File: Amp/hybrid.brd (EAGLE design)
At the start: 172.7 x 137.2 mm, 139 parts, among them IC1 TL071P, IC2 TL071P, IC3 LM317MABT, IC4 LM317MABT, J1 NRJ3HF-1, K1 UA2-12NJ, Q1 KSP06KINKED, Q10 BD139, Q11 KSP06KINKED, Q12 BC560KINKED, Q13 BC560KINKED, Q14 BC560KINKED, Q15 BC556KINKED, Q16 BC550KINKED, Q17 BC550KINKED, Q18 BC560KINKED, Q19 BD140, Q2 BC560KINKED, Q20 BD139, Q21 KSP43, Q22 KSP43, Q23 BC546KINKED, Q3 BC560KINKED, Q4 BC560KINKED, Q5 BC556KINKED, Q6 BC550KINKED, Q7 BC550KINKED, Q8 BC560KINKED, Q9 BD140, U1 TL7700DIP-8

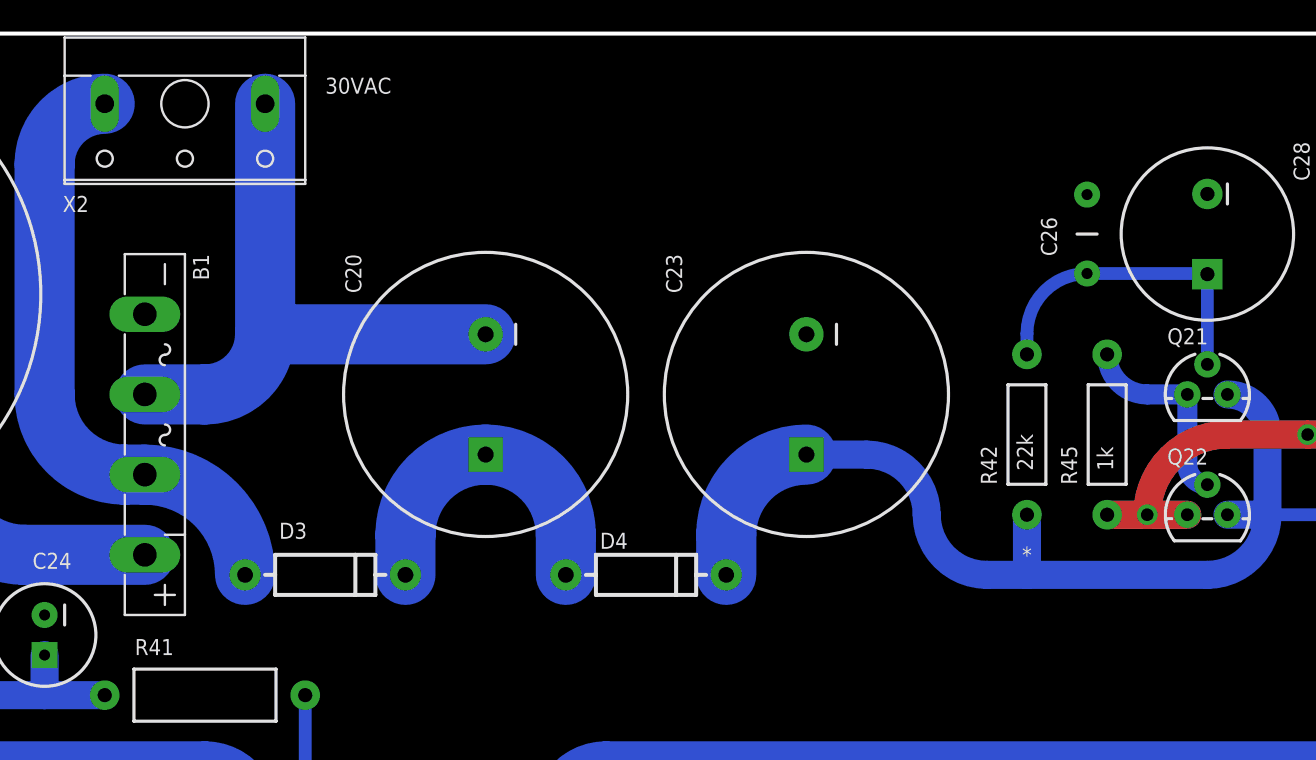
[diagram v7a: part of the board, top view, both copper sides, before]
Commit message: Use snap in caps
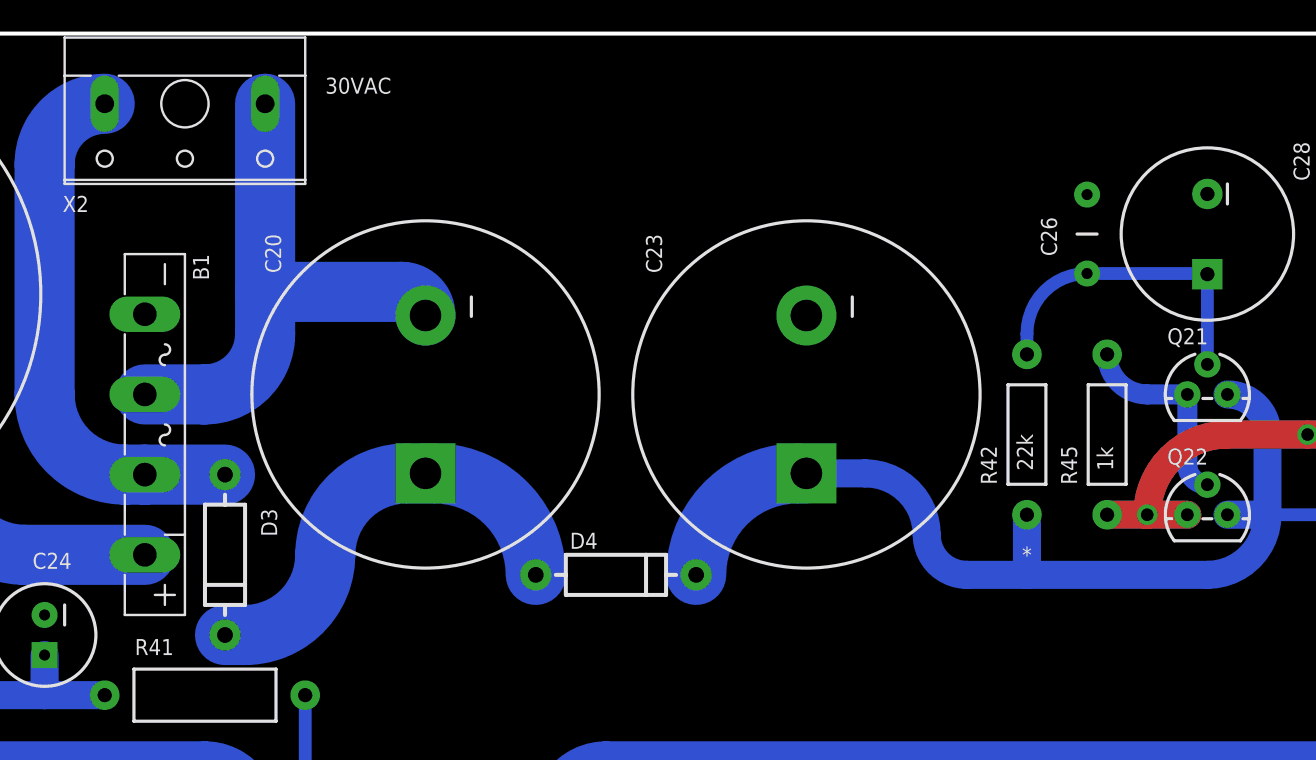
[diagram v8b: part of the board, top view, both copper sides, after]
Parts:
- C20, C23: device my-cap:CPOL-RADIAL-18/7.5 -> my-cap:CPOL-SNAPIN-22/10
- moved D3 6.48 mm to (74.9, 104.1), turned to 270 degrees
- moved C20 3.81 mm to (87.6, 114.3)
- moved D4 1.91 mm to (99.7, 102.9)
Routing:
- net N$31: track 19.4 -> 26.6 mm
- net AC_1: track 37.4 -> 33.5 mm
- net AC_2: track 37.8 -> 34.6 mm
- net N$33: track 74.5 -> 73.9 mm
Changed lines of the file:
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@@
 <attribute name="VALUE" x="135.255" y="17.272" size="1.016" layer="27" ratio="19"/>
 </element>
-<element name="C20" library="my-cap" package="CPOL-RADIAL-18/7.5" value="470uF" x="91.44" y="114.3" smashed="yes" rot="R270">
-<attribute name="NAME" x="82.55" y="123.19" size="1.016" layer="25" ratio="19" rot="R270"/>
-<attribute name="VALUE" x="95.25" y="116.84" size="1.016" layer="27" ratio="19" rot="R270"/>
-</element>
-<element name="C23" library="my-cap" package="CPOL-RADIAL-18/7.5" value="470uF" x="111.76" y="114.3" smashed="yes" rot="R270">
-<attribute name="NAME" x="102.87" y="123.19" size="1.016" layer="25" ratio="19" rot="R270"/>
+<element name="C20" library="my-cap" package="CPOL-SNAPIN-22/10" value="470uF" x="87.63" y="114.3" smashed="yes" rot="R270">
+<attribute name="NAME" x="77.47" y="124.46" size="1.016" layer="25" ratio="19" rot="R270"/>
+<attribute name="VALUE" x="91.44" y="116.84" size="1.016" layer="27" ratio="19" rot="R270"/>
+</element>
+<element name="C23" library="my-cap" package="CPOL-SNAPIN-22/10" value="470uF" x="111.76" y="114.3" smashed="yes" rot="R270">
+<attribute name="NAME" x="101.6" y="124.46" size="1.016" layer="25" ratio="19" rot="R270"/>
 <attribute name="VALUE" x="115.57" y="116.84" size="1.016" layer="27" ratio="19" rot="R270"/>
 </element>
@@
 <attribute name="VALUE" x="37.465" y="11.938" size="1.016" layer="27" ratio="19" rot="R180"/>
 </element>
-<element name="D3" library="SparkFun-DiscreteSemi" package="DIODE-1N4001" value="" x="81.28" y="102.87" smashed="yes">
-<attribute name="NAME" x="78.359" y="105.156" size="1.016" layer="25" ratio="19"/>
-<attribute name="VALUE" x="78.359" y="102.362" size="1.016" layer="21" ratio="12"/>
+<element name="D3" library="SparkFun-DiscreteSemi" package="DIODE-1N4001" value="" x="74.93" y="104.14" smashed="yes" rot="R270">
+<attribute name="NAME" x="77.216" y="107.061" size="1.016" layer="25" ratio="19" rot="R270"/>
+<attribute name="VALUE" x="74.422" y="107.061" size="1.016" layer="21" ratio="12" rot="R270"/>
 </element>
 <element name="D9" library="SparkFun-DiscreteSemi" package="DIODE-1N4001" value="" x="161.29" y="123.19" smashed="yes">
@@
 <attribute name="VALUE" x="158.369" y="122.682" size="1.016" layer="21" ratio="12"/>
 </element>
-<element name="D4" library="SparkFun-DiscreteSemi" package="DIODE-1N4001" value="" x="101.6" y="102.87" smashed="yes">
-<attribute name="NAME" x="98.679" y="104.521" size="1.016" layer="25" ratio="19"/>
-<attribute name="VALUE" x="98.679" y="102.362" size="1.016" layer="21" ratio="12"/>
+<element name="D4" library="SparkFun-DiscreteSemi" package="DIODE-1N4001" value="" x="99.695" y="102.87" smashed="yes">
+<attribute name="NAME" x="96.774" y="104.521" size="1.016" layer="25" ratio="19"/>
+<attribute name="VALUE" x="96.774" y="102.362" size="1.016" layer="21" ratio="12"/>
 </element>
 <element name="D7" library="SparkFun-DiscreteSemi" package="DIODE-1N4001" value="" x="161.29" y="105.41" smashed="yes" rot="R180">
@@
 <contactref element="D4" pad="A"/>
 <contactref element="C20" pad="1"/>
-<wire x1="91.44" y1="110.49" x2="96.52" y2="105.41" width="3.81" layer="16" curve="-90"/>
-<wire x1="96.52" y1="105.41" x2="96.52" y2="102.87" width="3.81" layer="16"/>
-<wire x1="86.36" y1="102.87" x2="86.36" y2="105.41" width="3.81" layer="16"/>
-<wire x1="86.36" y1="105.41" x2="91.44" y2="110.49" width="3.81" layer="16" curve="-90"/>
+<wire x1="74.93" y1="99.06" x2="76.2" y2="99.06" width="3.81" layer="16"/>
+<wire x1="76.2" y1="99.06" x2="81.28" y2="104.14" width="3.81" layer="16" curve="90"/>
+<wire x1="86.44" y1="109.3" x2="81.28" y2="104.14" width="3.81" layer="16" curve="90"/>
+<wire x1="87.63" y1="109.3" x2="86.44" y2="109.3" width="3.81" layer="16"/>
+<wire x1="94.615" y1="102.87" x2="88.185" y2="109.3" width="3.81" layer="16" curve="90"/>
+<wire x1="88.185" y1="109.3" x2="87.63" y2="109.3" width="3.81" layer="16"/>
 </signal>
 <signal name="N$33" class="2">
@@
 <contactref element="D7" pad="C"/>
 <contactref element="Q21" pad="3"/>
-<wire x1="106.68" y1="102.87" x2="106.68" y2="105.41" width="3.81" layer="16"/>
-<wire x1="111.76" y1="110.49" x2="106.68" y2="105.41" width="3.81" layer="16" curve="90"/>
 <wire x1="140.97" y1="106.68" x2="138.43" y2="106.68" width="1.778" layer="16"/>
 <wire x1="140.97" y1="106.68" x2="140.97" y2="111.76" width="1.778" layer="16"/>
 <wire x1="140.97" y1="111.76" x2="138.43" y2="114.3" width="1.778" layer="16" curve="90"/>
 <wire x1="140.97" y1="106.68" x2="137.16" y2="102.87" width="1.778" layer="16" curve="-90"/>
-<wire x1="123.19" y1="102.87" x2="119.38" y2="106.68" width="1.778" layer="16" curve="-90"/>
-<wire x1="119.38" y1="106.68" x2="115.57" y2="110.49" width="1.778" layer="16" curve="90"/>
-<wire x1="115.57" y1="110.49" x2="111.76" y2="110.49" width="1.778" layer="16"/>
-<wire x1="125.73" y1="102.87" x2="137.16" y2="102.87" width="1.778" layer="16"/>
-<wire x1="125.73" y1="102.87" x2="123.19" y2="102.87" width="1.778" layer="16"/>
+<wire x1="137.16" y1="102.87" x2="125.73" y2="102.87" width="1.778" layer="16"/>
 <wire x1="125.73" y1="106.68" x2="125.73" y2="102.87" width="1.778" layer="16"/>
 <wire x1="156.21" y1="105.41" x2="154.94" y2="106.68" width="0.8128" layer="16" curve="90"/>
 <wire x1="154.94" y1="106.68" x2="140.97" y2="106.68" width="0.8128" layer="16"/>
+<wire x1="104.775" y1="102.87" x2="111.205" y2="109.3" width="3.81" layer="16" curve="-90"/>
+<wire x1="111.76" y1="109.3" x2="111.205" y2="109.3" width="3.81" layer="16"/>
+<wire x1="125.73" y1="102.87" x2="121.92" y2="102.87" width="1.778" layer="16"/>
+<wire x1="121.92" y1="102.87" x2="119.38" y2="105.41" width="1.778" layer="16" curve="-90"/>
+<wire x1="119.38" y1="105.41" x2="115.49" y2="109.3" width="1.778" layer="16" curve="90"/>
+<wire x1="115.49" y1="109.3" x2="111.76" y2="109.3" width="1.778" layer="16"/>
 </signal>
 <signal name="N$36">
@@
 <wire x1="69.85" y1="114.3" x2="73.66" y2="114.3" width="3.81" layer="16"/>
 <wire x1="77.47" y1="118.11" x2="73.66" y2="114.3" width="3.81" layer="16" curve="-90"/>
-<wire x1="77.47" y1="118.11" x2="77.47" y2="132.715" width="3.81" layer="16"/>
-<wire x1="91.44" y1="118.11" x2="77.47" y2="118.11" width="3.81" layer="16"/>
+<wire x1="77.47" y1="120.797778125" x2="77.47" y2="118.11" width="3.81" layer="16"/>
+<wire x1="77.47" y1="120.797778125" x2="77.47" y2="132.715" width="3.81" layer="16"/>
+<wire x1="87.63" y1="119.3" x2="86.132221875" y2="120.797778125" width="3.81" layer="16" curve="90"/>
+<wire x1="86.132221875" y1="120.797778125" x2="77.47" y2="120.797778125" width="3.81" layer="16"/>
 </signal>
 <signal name="AC_1">
@@
 <wire x1="63.5" y1="128.905" x2="67.31" y2="132.715" width="3.81" layer="16" curve="-90"/>
 <wire x1="63.5" y1="114.3" x2="63.5" y2="128.905" width="3.81" layer="16"/>
-<wire x1="76.2" y1="102.87" x2="69.85" y2="109.22" width="3.81" layer="16" curve="90"/>
-<wire x1="69.85" y1="109.22" x2="68.58" y2="109.22" width="3.81" layer="16"/>
+<wire x1="68.58" y1="109.22" x2="69.85" y2="109.22" width="3.81" layer="16"/>
 <wire x1="68.58" y1="109.22" x2="63.5" y2="114.3" width="3.81" layer="16" curve="-90"/>
+<wire x1="69.85" y1="109.22" x2="74.93" y2="109.22" width="3.81" layer="16"/>
 </signal>
 <signal name="N$46">
